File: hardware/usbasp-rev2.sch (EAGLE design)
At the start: 29 parts, among them IC1 ATMEGA8-16A, U1 MIC2551, X1 USB-A-H, Y1 12MHz

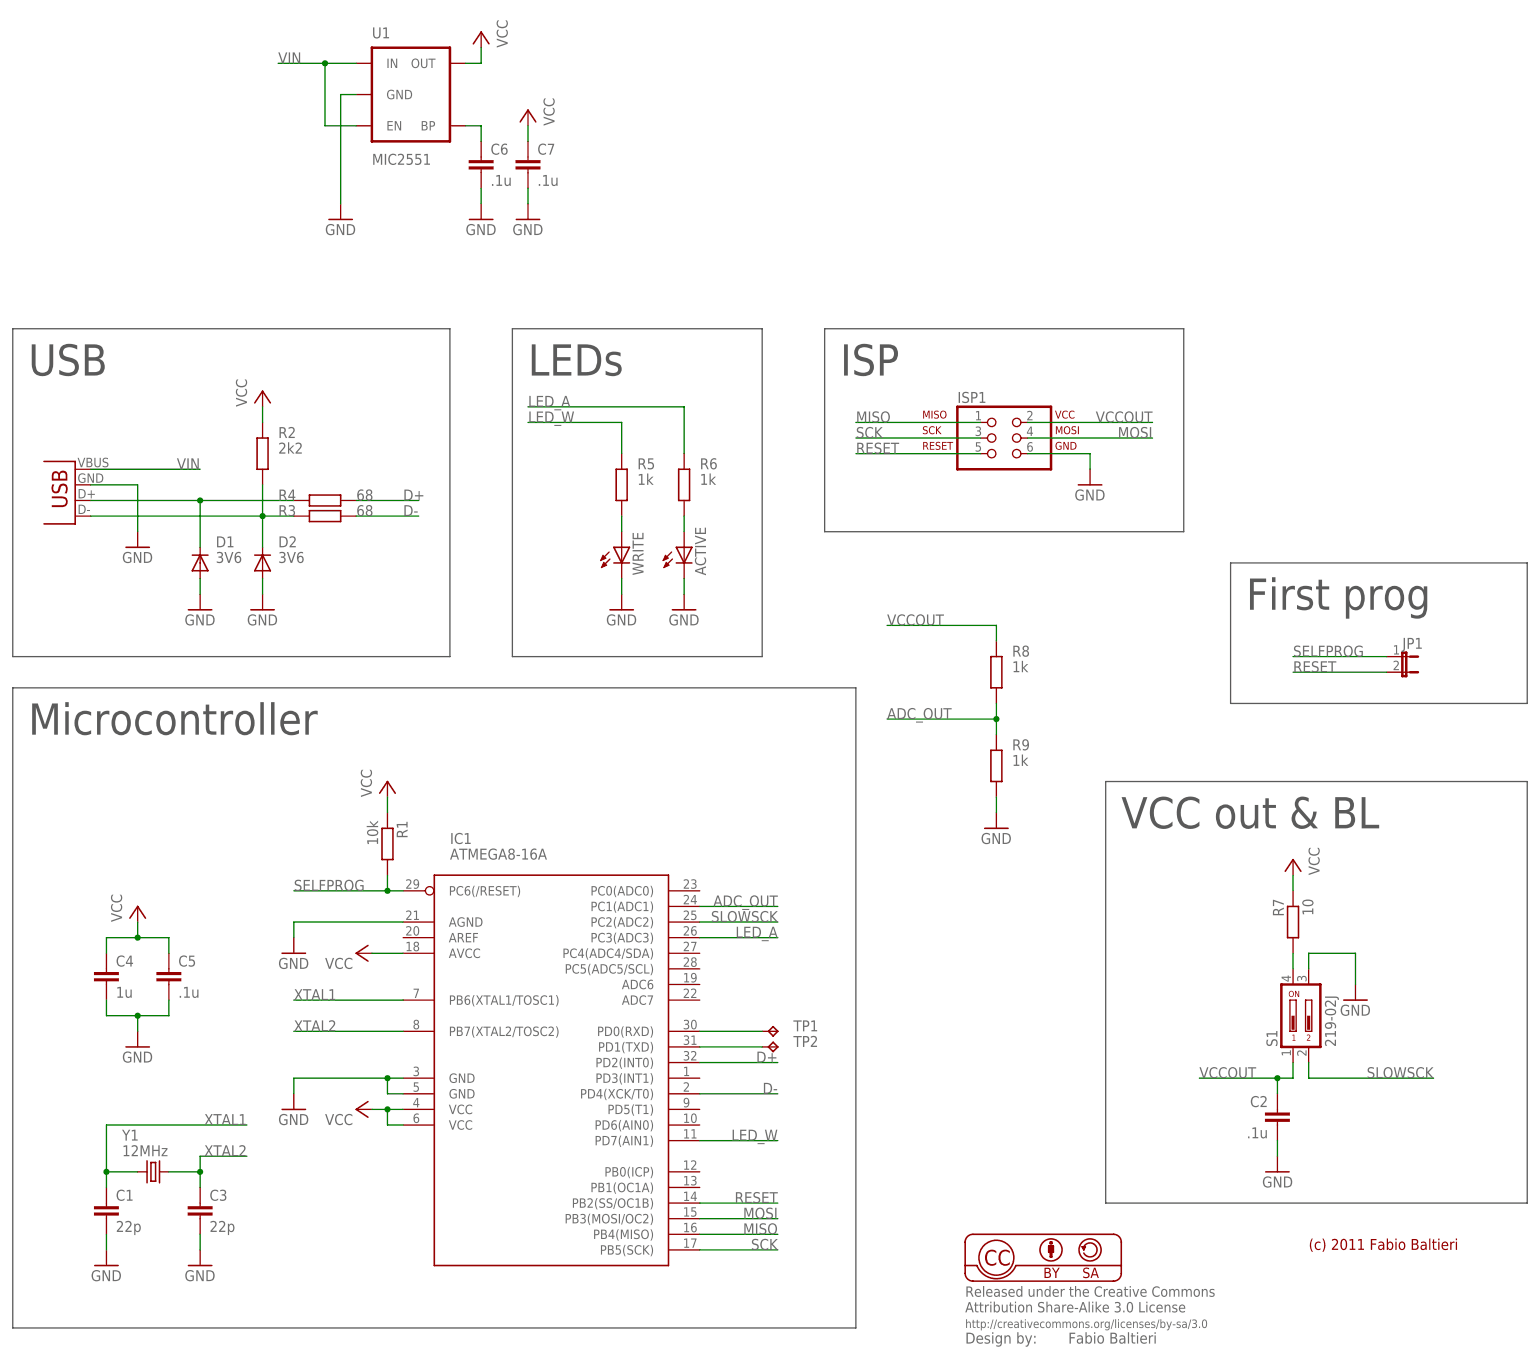
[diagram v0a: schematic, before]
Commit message: hw: updated rev2 schematics
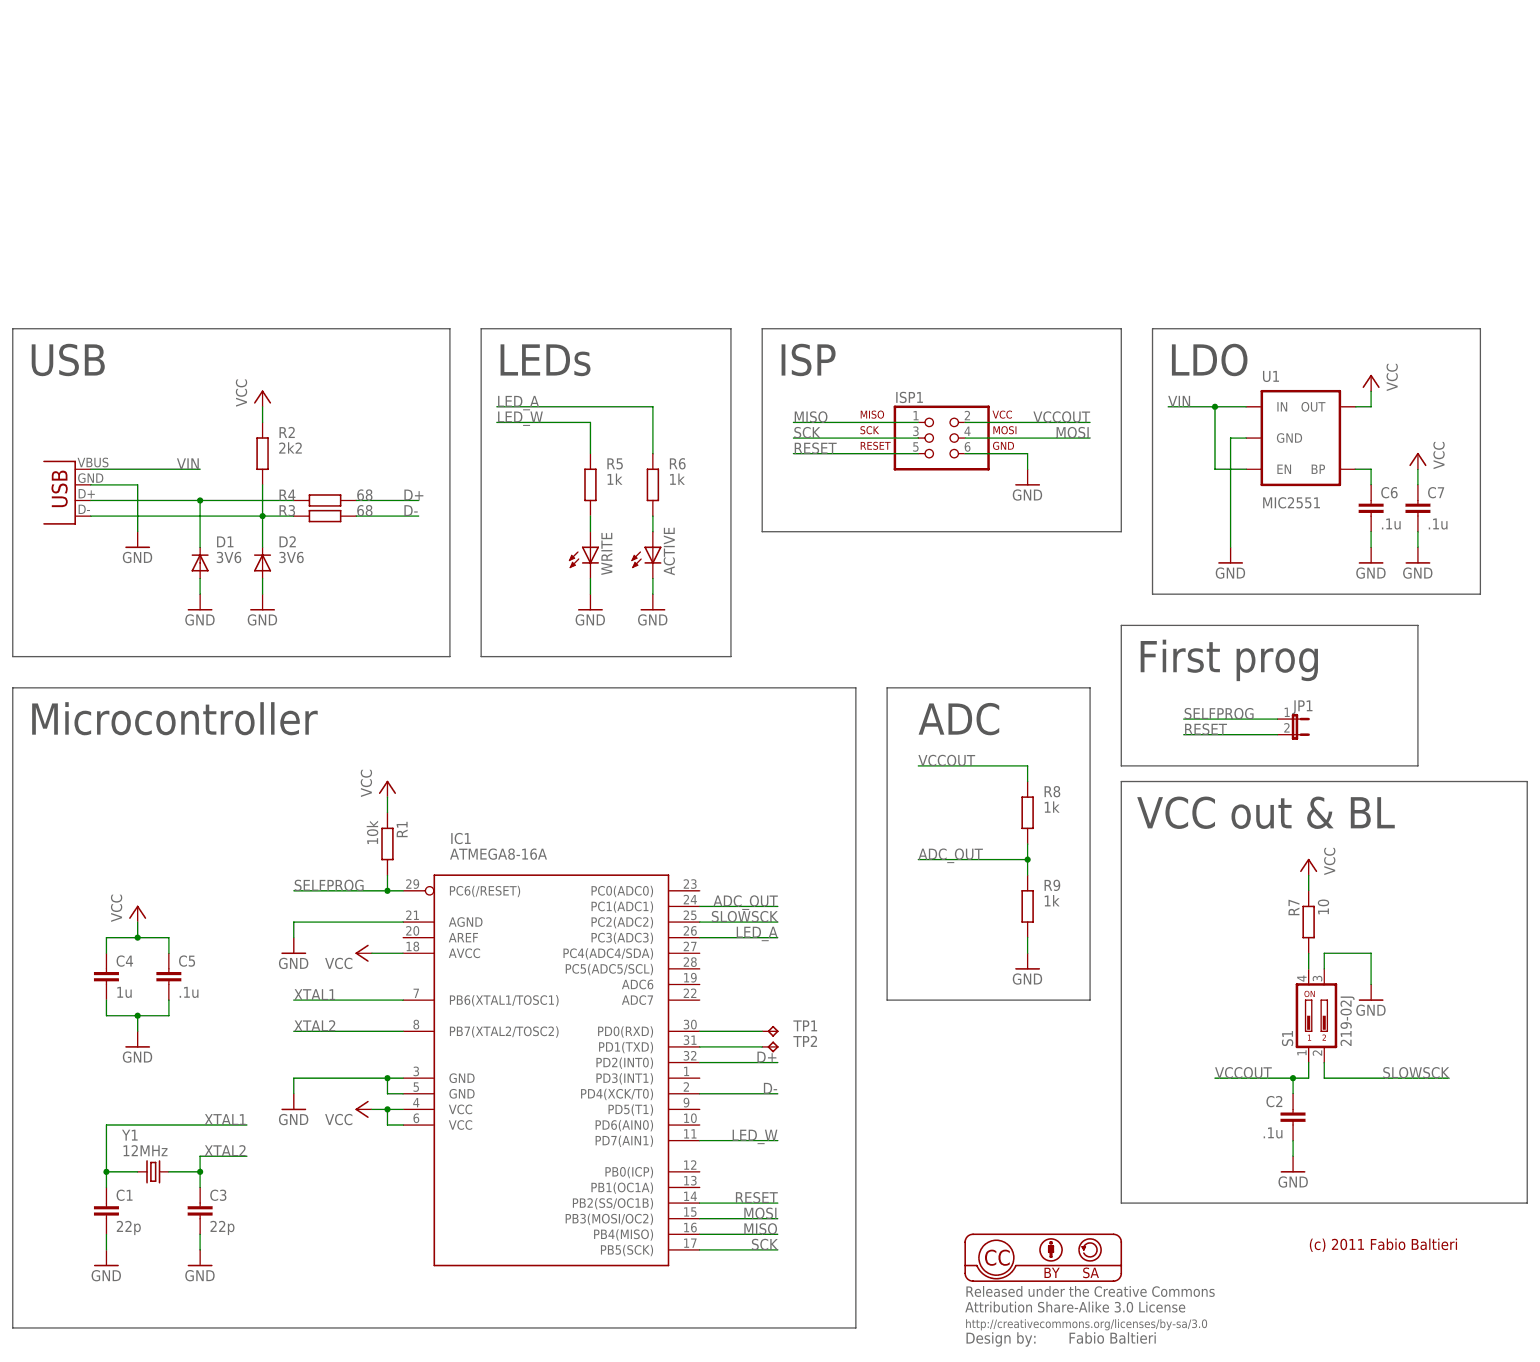
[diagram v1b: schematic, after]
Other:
- note added: "ADC"
- note added: "LDO"
- moved on the sheet: ACTIVE, C2, C6, C7, ISP1, JP1, R5, R6, R7, R8, R9, S1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

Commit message: hw: rev2: fix ldo part number
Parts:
- U1: value MIC2551 -> MIC5301
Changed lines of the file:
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@@
 <part name="GND9" library="supply1" deviceset="GND" device=""/>
 <part name="GND11" library="supply1" deviceset="GND" device=""/>
-<part name="U1" library="SparkFun-PowerIC" deviceset="V_REG_LDO" device="SMD" value="MIC2551"/>
+<part name="U1" library="SparkFun-PowerIC" deviceset="V_REG_LDO" device="SMD" value="MIC5301"/>
 <part name="P+9" library="supply1" deviceset="VCC" device=""/>
 <part name="GND12" library="supply1" deviceset="GND" device=""/>

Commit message: hw: update part values
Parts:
- ACTIVE: value (none) -> RED
- R5, R6: value 1k -> 470
- R7: value 10 -> 1
- R8: value 1k -> 4k7
- WRITE: value (none) -> GREEN
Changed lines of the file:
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@@
 <?xml version="1.0" encoding="utf-8"?>
 <!DOCTYPE eagle SYSTEM "eagle.dtd">
-<eagle version="6.3">
+<eagle version="6.4">
 <drawing>
 <settings>
@@
 <part name="P+4" library="supply1" deviceset="VCC" device=""/>
 <part name="C5" library="rcl" deviceset="C-EU" device="C0603" value=".1u"/>
-<part name="WRITE" library="led" deviceset="LED" device="CHIP-LED0805"/>
-<part name="ACTIVE" library="led" deviceset="LED" device="CHIP-LED0805"/>
+<part name="WRITE" library="led" deviceset="LED" device="CHIP-LED0805" value="GREEN"/>
+<part name="ACTIVE" library="led" deviceset="LED" device="CHIP-LED0805" value="RED"/>
 <part name="GND4" library="supply1" deviceset="GND" device=""/>
-<part name="R5" library="rcl" deviceset="R-EU_" device="R0603" value="1k"/>
-<part name="R6" library="rcl" deviceset="R-EU_" device="R0603" value="1k"/>
+<part name="R5" library="rcl" deviceset="R-EU_" device="R0603" value="470"/>
+<part name="R6" library="rcl" deviceset="R-EU_" device="R0603" value="470"/>
 <part name="GND8" library="supply1" deviceset="GND" device=""/>
 <part name="GND10" library="supply1" deviceset="GND" device=""/>
@@
 <part name="TP1" library="testpad" deviceset="TP" device="B1,27"/>
 <part name="TP2" library="testpad" deviceset="TP" device="B1,27"/>
-<part name="R7" library="rcl" deviceset="R-EU_" device="R0805" value="10"/>
+<part name="R7" library="rcl" deviceset="R-EU_" device="R0805" value="1"/>
 <part name="LICENSE1" library="balto" deviceset="CC_BY-SA" device="" value="Fabio Baltieri"/>
 <part name="GND5" library="supply1" deviceset="GND" device=""/>
@@
 <part name="JP1" library="SparkFun-Passives" deviceset="JUMPER-2" device="SMD-NO-NS"/>
 <part name="S1" library="switch-dil" deviceset="219-02*" device="J"/>
-<part name="R8" library="rcl" deviceset="R-EU_" device="R0603" value="1k"/>
+<part name="R8" library="rcl" deviceset="R-EU_" device="R0603" value="4k7"/>
 <part name="R9" library="rcl" deviceset="R-EU_" device="R0603" value="1k"/>
 <part name="GND17" library="supply1" deviceset="GND" device=""/>
